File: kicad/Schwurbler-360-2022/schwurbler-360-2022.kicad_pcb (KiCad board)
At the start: 2 copper layers, 121.9 x 118.1 mm, 53 parts, among them IC1 MCP23017_SP, SW1 SW_Push, SW2 SW_Push, SW3 SW_Push, SW4 SW_Push, SW5 SW_Push, SW6 SW_Push, SW7 SW_Push, SW8 SW_Push

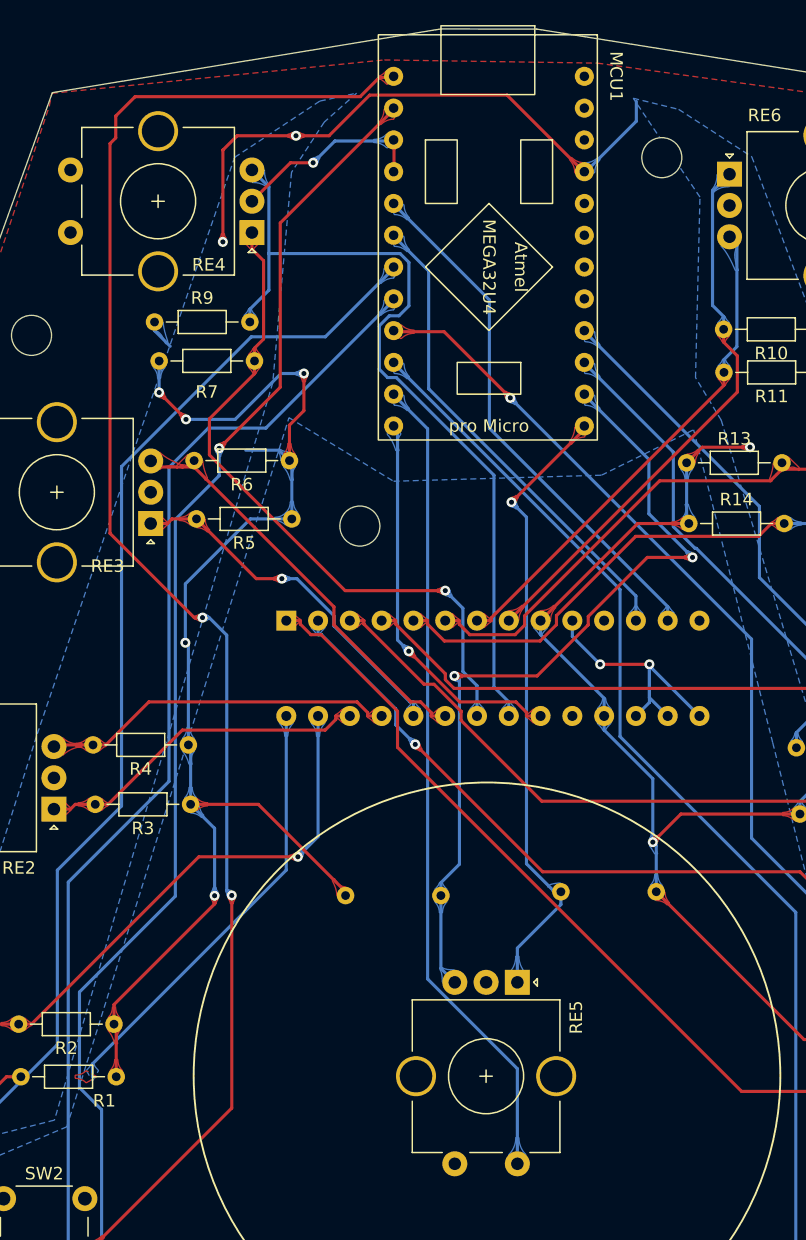
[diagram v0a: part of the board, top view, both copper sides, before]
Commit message: Add files via upload
Fixed connections to Pins 1, 11, 12, 13 and 23 of the Arduino Pro Micro.
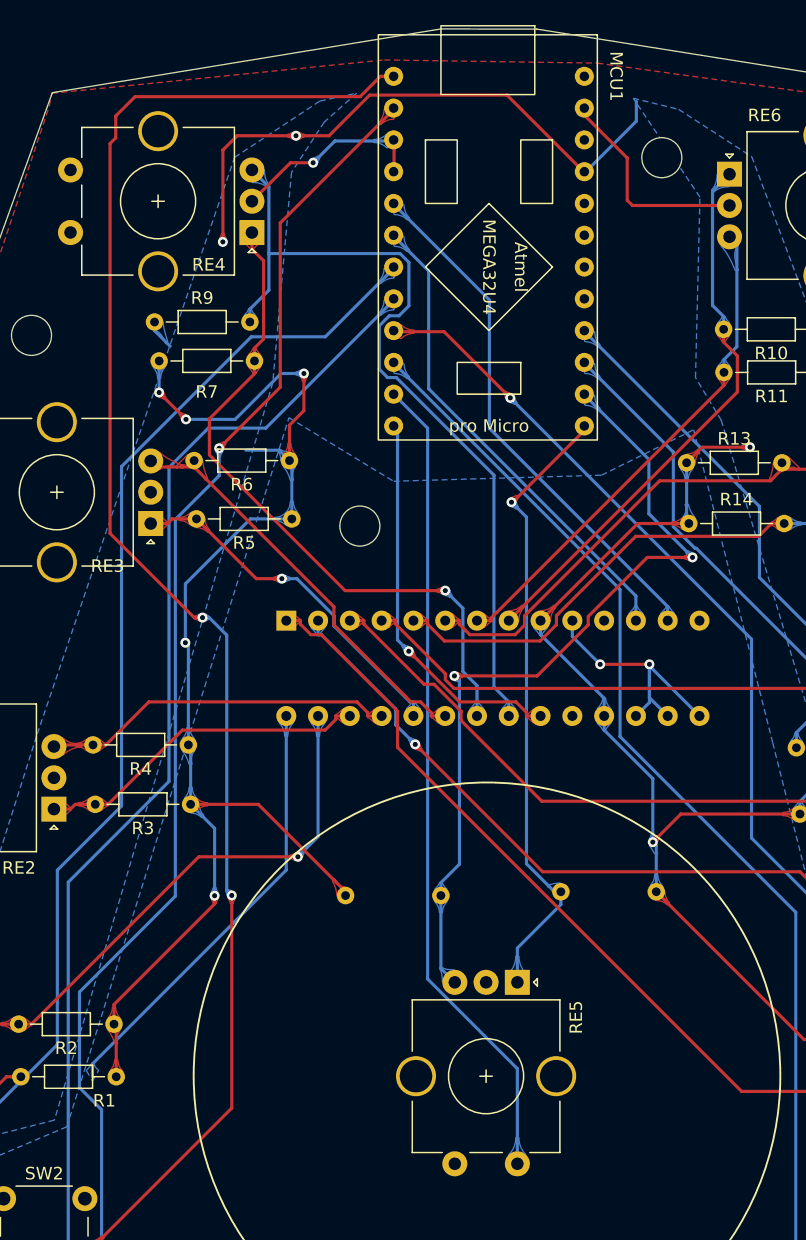
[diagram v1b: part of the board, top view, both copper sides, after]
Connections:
- MCU1 pad 1: (no net) -> /Push_2
- MCU1 pad 11: (no net) -> /RE_Push
- MCU1 pad 12: (no net) -> /PWM
- MCU1 pad 13: (no net) -> /RE5_DT
- MCU1 pad 21: (no net) -> /5V
- MCU1 pad 23: (no net) -> /GND
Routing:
- net /GND: track 39.5 -> 56.6 mm
